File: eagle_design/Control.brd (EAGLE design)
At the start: 55.9 x 63.2 mm, 17 parts, among them K1 G5LE, K2 G5LE, K3 G5LE

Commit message: Did some more PCB design and added some datasheets
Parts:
- removed B1: RECTIFIER-S80, rectifier:TO-269AA
- removed D1, D2, D3: 1N4148DO35-7, diode:DO35-7
- removed D8: CGRM4001-G, diode:SOD-123_MINI-SMA
- removed K1, K2, K3: G5LE, relay:G5LE
- removed SV3, SV4: (no value), con-lstb:MA05-1
- removed T1, T2, T3: (no value), transistor-neu-to92:TO92-EBC
- removed VREG-3.3: (no value), linear-technology:SOT223
- removed VREG-5: TL2575-05, texas:TO-263-5
- added C3, C4: 10uF, rcl:C0805
- added MSP430F1232: F12X2---DW28, TI_MSP430_v16:DW28
- added RN-131C: RN-131G, SparkFun:RN-131G
- added SV1: (no value), con-lstb:MA05-1
- C1: value 100uF -> 0.1uF; device rcl:153CLV-0405 -> rcl:C0805
- C2: value 330uF -> 0.1uF; device rcl:153CLV-0405 -> rcl:C0805
- moved C2 41.5 mm to (36.8, 2.54), turned to 270 degrees
- moved C1 31.9 mm to (5.08, 22.9), turned to 270 degrees
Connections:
- removed net 3.3+: SV3.5, VREG-3.3.3
- removed net 5V+: C2.+, D1.C, D2.C, D3.C, K1.1, K2.1, K3.1, VREG-3.3.1, VREG-5.4
- removed net G: K3.S, SV4.1
- removed net N$1: B1.+, C1.+, VREG-5.1
- removed net N$2: D1.A, K3.2, T1.C
- removed net N$3: D2.A, K2.2, T2.C
- removed net N$4: D8.C, VREG-5.2
- removed net N$5: D3.A, K1.2, T3.C
- removed net N$6: K1.O
- removed net N$7: K2.O
- removed net N$8: K3.O
- removed net VAC+: B1.AC1, K1.P, K2.P, K3.P, SV4.5
- removed net VAC-: SV4.4
- removed net W: K1.S, SV4.3
- removed net Y: K2.S, SV4.2
- new net RESET: RN-131C.RESET
- new net RN-RX: MSP430F1232.15, RN-131C.UART-RX
- new net RN-TX: MSP430F1232.16, RN-131C.UART-TX
- new net VCC: C1.1, C2.1, C3.1, C4.1, MSP430F1232.2, RN-131C.VDD-BATT, RN-131C.VDD-IN, SV1.5
- net AC: now also SV1.2; no longer SV3.2, T2.B
- net FAN: now also SV1.1; no longer SV3.1, T1.B
- net GND: now also C1.2, C2.2, C3.2, C4.2, MSP430F1232.4, RN-131C.3.3-RIN, RN-131C.GND0, RN-131C.GND1, RN-131C.GND2, RN-131C.GND3, RN-131C.GND4, RN-131C.GND5, RN-131C.GND6, RN-131C.GND7, RN-131C.GND8, RN-131C.GND9, SV1.4; no longer B1.-, C1.-, C2.-, D8.A, SV3.4, T1.E, T2.E, T3.E, VREG-3.3.2, VREG-3.3.4, VREG-5.3, VREG-5.5, VREG-5.TAB
- net HEAT: now also SV1.3; no longer SV3.3, T3.B
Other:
- board size 55.9 x 63.2 mm -> 45.7 x 36.5 mm

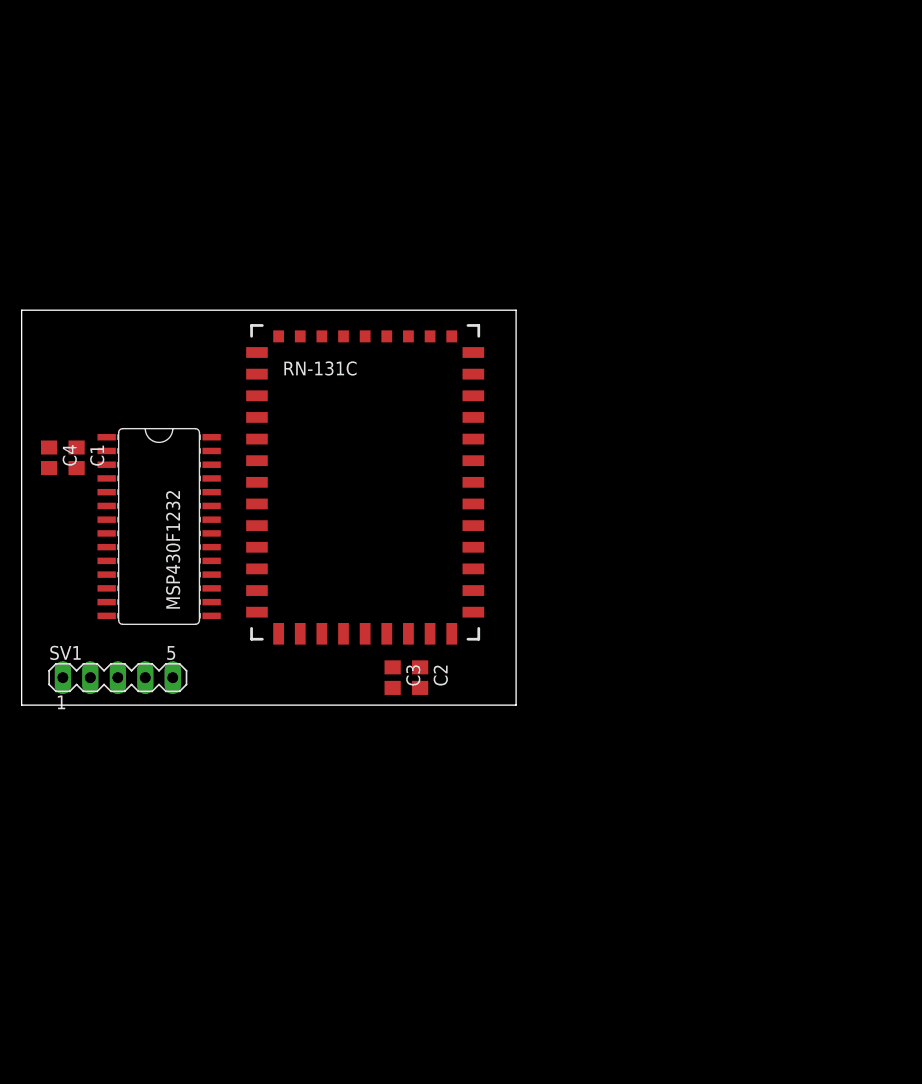
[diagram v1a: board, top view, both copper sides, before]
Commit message: split into three boards and choose new mcu
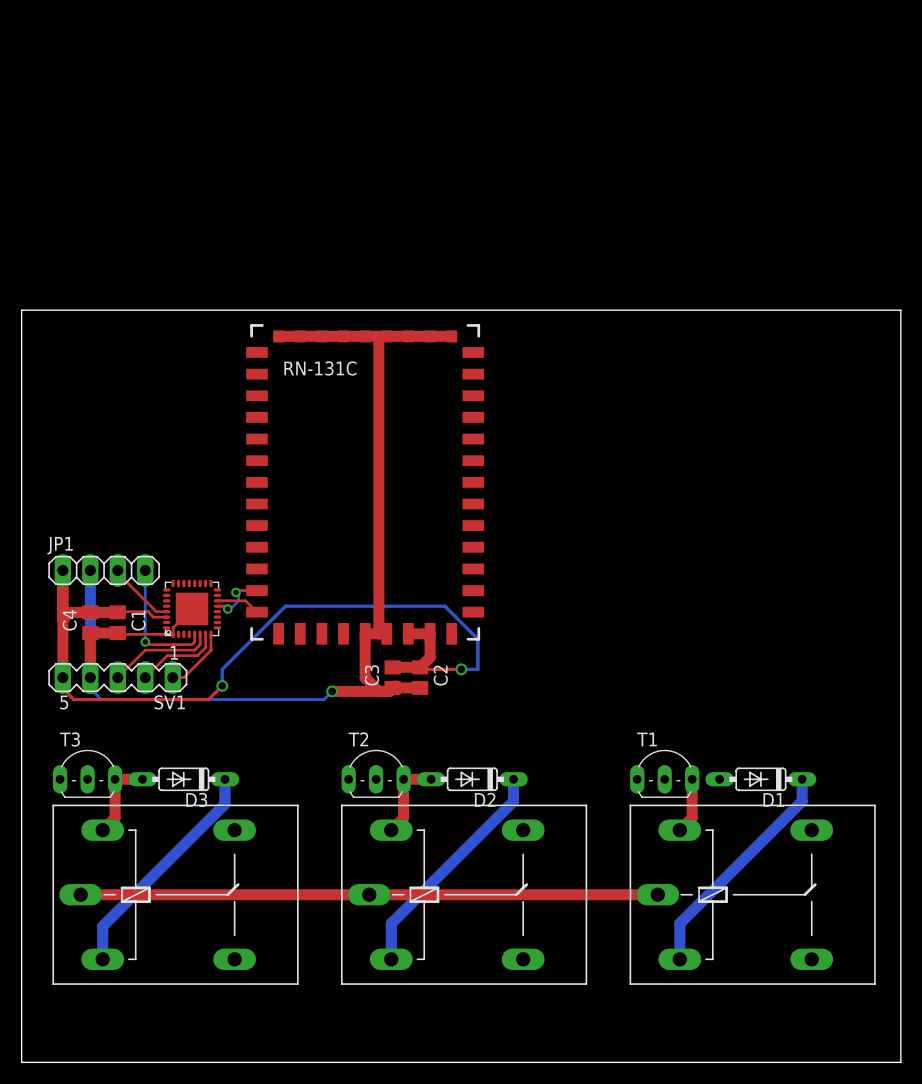
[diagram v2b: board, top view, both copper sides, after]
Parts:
- removed MSP430F1232: F12X2---DW28, TI_MSP430_v16:DW28
- added D1, D2, D3: 1N4148DO35-7, diode:DO35-7
- added JP1: (no value), pinhead:1X04
- added K1, K2, K3: G5LE, relay:G5LE
- added T1, T2, T3: (no value), transistor-neu-to92:TO92-EBC
- added U$1: F21X2---RHB32, TI_MSP430_v16:RHB32
- moved C1 15.7 mm to (8.89, 7.62)
- moved C4 15.7 mm to (6.35, 7.62)
- turned SV1 to 180 degrees
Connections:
- new net 5V+: D1.C, D2.C, D3.C, K1.1, K2.1, K3.1
- new net G: K3.S
- new net N$2: D1.A, K3.2, T1.C
- new net N$3: D2.A, K2.2, T2.C
- new net N$5: D3.A, K1.2, T3.C
- new net N$6: K1.O
- new net N$7: K2.O
- new net N$8: K3.O
- new net RST: JP1.4, U$1.5
- new net TEST: JP1.3, U$1.29
- new net VAC+: K1.P, K2.P, K3.P
- new net W: K1.S
- new net Y: K2.S
- net AC: now also T2.B, U$1.7
- net FAN: now also T1.B, U$1.8
- net GND: now also JP1.2, T1.E, T2.E, T3.E, U$1.1, U$1.TP; no longer MSP430F1232.4
- net HEAT: now also T3.B, U$1.6
- net RN-RX: now also U$1.13; no longer MSP430F1232.15
- net RN-TX: now also U$1.14; no longer MSP430F1232.16
- net VCC: now also JP1.1, U$1.30; no longer MSP430F1232.2
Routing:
- net GND: track 0.00 -> 110.3 mm, vias 0 -> 1
- net VCC: track 0.00 -> 86.0 mm, vias 0 -> 2
- net 5V+: track 0.00 -> 64.0 mm
- net VAC+: track 0.00 -> 53.3 mm
- net RST: track 0.00 -> 12.1 mm, vias 0 -> 1
- net HEAT: track 0.00 -> 9.83 mm
- net AC: track 0.00 -> 7.96 mm
- net N$5: track 0.00 -> 7.71 mm
- net N$3: track 0.00 -> 7.71 mm
- net TEST: track 0.00 -> 6.24 mm
- net FAN: track 0.00 -> 6.08 mm
- net RN-RX: track 0.00 -> 5.27 mm, vias 0 -> 2
- net N$2: track 0.00 -> 5.17 mm
- net RN-TX: track 0.00 -> 4.09 mm
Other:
- board size 45.7 x 36.5 mm -> 81.3 x 69.5 mm

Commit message: removed relays from control
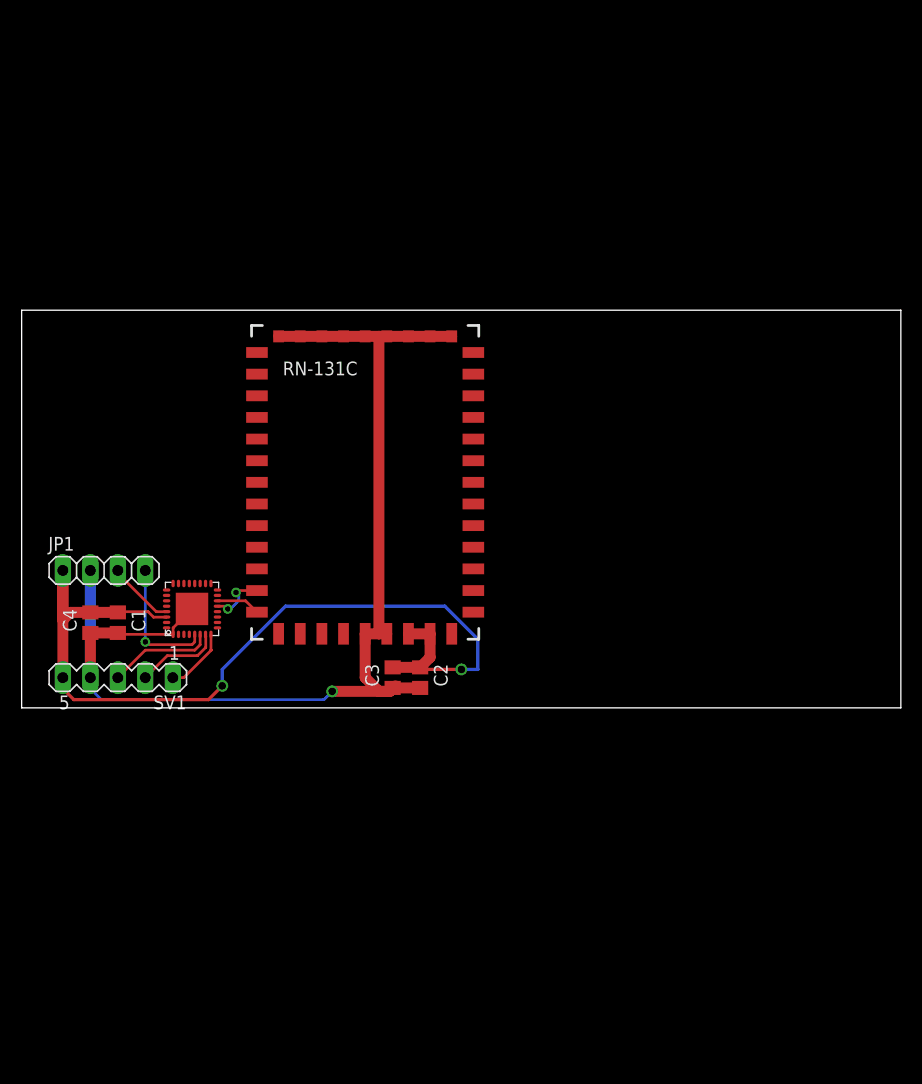
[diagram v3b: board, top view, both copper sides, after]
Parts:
- removed D1, D2, D3: 1N4148DO35-7, diode:DO35-7
- removed K1, K2, K3: G5LE, relay:G5LE
- removed T1, T2, T3: (no value), transistor-neu-to92:TO92-EBC
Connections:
- removed net 5V+: D1.C, D2.C, D3.C, K1.1, K2.1, K3.1
- removed net G: K3.S
- removed net N$2: D1.A, K3.2, T1.C
- removed net N$3: D2.A, K2.2, T2.C
- removed net N$5: D3.A, K1.2, T3.C
- removed net N$6: K1.O
- removed net N$7: K2.O
- removed net N$8: K3.O
- removed net VAC+: K1.P, K2.P, K3.P
- removed net W: K1.S
- removed net Y: K2.S
- net AC: no longer T2.B
- net FAN: no longer T1.B
- net GND: no longer T1.E, T2.E, T3.E
- net HEAT: no longer T3.B
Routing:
- net 5V+: track 64.0 -> 0.00 mm
- net VAC+: track 53.3 -> 0.00 mm
- net N$5: track 7.71 -> 0.00 mm
- net N$3: track 7.71 -> 0.00 mm
- net N$2: track 5.17 -> 0.00 mm
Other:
- board size 81.3 x 69.5 mm -> 81.3 x 36.8 mm
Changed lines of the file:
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@@
 <board>
 <plain>
-<wire x1="0" y1="-33.02" x2="81.26" y2="-33.02" width="0" layer="20"/>
-<wire x1="81.26" y1="-33.02" x2="81.26" y2="36.5" width="0" layer="20"/>
+<wire x1="0" y1="-0.254" x2="81.26" y2="-0.254" width="0" layer="20"/>
+<wire x1="81.26" y1="-0.254" x2="81.26" y2="36.5" width="0" layer="20"/>
 <wire x1="81.26" y1="36.5" x2="0" y2="36.5" width="0" layer="20"/>
-<wire x1="0" y1="36.5" x2="0" y2="-33.02" width="0" layer="20"/>
+<wire x1="0" y1="36.5" x2="0" y2="-0.254" width="0" layer="20"/>
 </plain>
 <attributes>
@@
 <element name="U$1" library="TI_MSP430_v16" package="RHB32" value="F21X2---RHB32" x="15.748" y="8.89" smashed="yes" rot="R90"/>
 <element name="JP1" library="pinhead" package="1X04" value="" x="7.62" y="12.446"/>
-<element name="K1" library="relay" package="G5LE" value="G5LE" x="14.986" y="-17.526" smashed="yes">
-<attribute name="OC_NEWARK" value="unknown" x="14.986" y="-17.526" size="1.778" layer="27" display="off"/>
-<attribute name="MPN" value="" x="14.986" y="-17.526" size="1.778" layer="27" display="off"/>
-<attribute name="MF" value="" x="14.986" y="-17.526" size="1.778" layer="27" display="off"/>
-<attribute name="OC_FARNELL" value="unknown" x="14.986" y="-17.526" size="1.778" layer="27" display="off"/>
-</element>
-<element name="K2" library="relay" package="G5LE" value="G5LE" x="41.656" y="-17.526" smashed="yes">
-<attribute name="OC_NEWARK" value="unknown" x="41.656" y="-17.526" size="1.778" layer="27" display="off"/>
-<attribute name="MPN" value="" x="41.656" y="-17.526" size="1.778" layer="27" display="off"/>
-<attribute name="MF" value="" x="41.656" y="-17.526" size="1.778" layer="27" display="off"/>
-<attribute name="OC_FARNELL" value="unknown" x="41.656" y="-17.526" size="1.778" layer="27" display="off"/>
-</element>
-<element name="K3" library="relay" package="G5LE" value="G5LE" x="68.326" y="-17.526" smashed="yes">
-<attribute name="OC_NEWARK" value="unknown" x="68.326" y="-17.526" size="1.778" layer="27" display="off"/>
-<attribute name="MPN" value="" x="68.326" y="-17.526" size="1.778" layer="27" display="off"/>
-<attribute name="MF" value="" x="68.326" y="-17.526" size="1.778" layer="27" display="off"/>
-<attribute name="OC_FARNELL" value="unknown" x="68.326" y="-17.526" size="1.778" layer="27" display="off"/>
-</element>
-<element name="D1" library="diode" package="DO35-7" value="1N4148DO35-7" x="68.326" y="-6.858" smashed="yes" rot="R180">
-<attribute name="NAME" x="70.612" y="-8.128" size="1.27" layer="25" ratio="10" rot="R180"/>
-</element>
-<element name="D2" library="diode" package="DO35-7" value="1N4148DO35-7" x="41.656" y="-6.858" smashed="yes" rot="R180">
-<attribute name="NAME" x="43.942" y="-8.128" size="1.27" layer="25" ratio="10" rot="R180"/>
-</element>
-<element name="D3" library="diode" package="DO35-7" value="1N4148DO35-7" x="14.986" y="-6.858" smashed="yes" rot="R180">
-<attribute name="NAME" x="17.272" y="-8.128" size="1.27" layer="25" ratio="10" rot="R180"/>
-</element>
-<element name="T1" library="transistor-neu-to92" package="TO92-EBC" value="" x="59.436" y="-5.588"/>
-<element name="T2" library="transistor-neu-to92" package="TO92-EBC" value="" x="32.766" y="-5.588"/>
-<element name="T3" library="transistor-neu-to92" package="TO92-EBC" value="" x="6.096" y="-5.588"/>
 </elements>
 <signals>
@@
 <wire x1="34.036" y1="1.27" x2="34.544" y2="1.778" width="1.016" layer="1"/>
 <wire x1="6.35" y1="12.446" x2="6.35" y2="2.54" width="1.016" layer="16"/>
-<contactref element="T1" pad="E"/>
-<contactref element="T2" pad="E"/>
-<contactref element="T3" pad="E"/>
 <wire x1="35.75" y1="34.082" x2="37.75" y2="34.082" width="0" layer="19" extent="1-1"/>
 <wire x1="33.75" y1="34.082" x2="35.75" y2="34.082" width="0" layer="19" extent="1-1"/>
@@
 <wire x1="27.75" y1="34.082" x2="29.75" y2="34.082" width="0" layer="19" extent="1-1"/>
 <wire x1="25.75" y1="34.082" x2="23.75" y2="34.082" width="0" layer="19" extent="1-1"/>
-<wire x1="30.226" y1="-6.858" x2="27.94" y2="0.508" width="0" layer="19" extent="16-16"/>
-<wire x1="3.556" y1="-6.858" x2="7.366" y2="0.508" width="0" layer="19" extent="16-16"/>
-<wire x1="56.896" y1="-6.858" x2="36.83" y2="1.59" width="0" layer="19" extent="1-1"/>
 </signal>
 <signal name="RESET">
@@
 <wire x1="16.002" y1="5.08" x2="11.43" y2="5.08" width="0.254" layer="1"/>
 <wire x1="11.43" y1="5.08" x2="8.89" y2="2.54" width="0.254" layer="1"/>
-<contactref element="T3" pad="B"/>
-<wire x1="6.096" y1="-6.858" x2="8.89" y2="2.54" width="0" layer="19" extent="1-1"/>
 </signal>
 <signal name="AC">
@@
 <wire x1="16.998" y1="6.54" x2="16.998" y2="6.37" width="0.254" layer="1"/>
 <wire x1="16.998" y1="6.37" x2="17.018" y2="6.35" width="0.254" layer="1"/>
-<contactref element="T2" pad="B"/>
-<wire x1="17.018" y1="5.334" x2="32.766" y2="-6.858" width="0" layer="19" extent="1-1"/>
 </signal>
 <signal name="FAN">
@@
 <wire x1="17.526" y1="5.08" x2="14.986" y2="2.54" width="0.254" layer="1"/>
 <wire x1="14.986" y1="2.54" x2="13.97" y2="2.54" width="0.254" layer="1"/>
-<contactref element="T1" pad="B"/>
-<wire x1="17.526" y1="5.08" x2="59.436" y2="-6.858" width="0" layer="19" extent="1-1"/>
 </signal>
 <signal name="TEST">
@@
 <wire x1="11.43" y1="5.842" x2="11.43" y2="12.446" width="0.254" layer="16"/>
 </signal>
-<signal name="N$2">
-<contactref element="D1" pad="A"/>
-<contactref element="K3" pad="2"/>
-<contactref element="T1" pad="C"/>
-<wire x1="61.976" y1="-6.858" x2="64.516" y2="-6.858" width="0" layer="19" extent="1-1"/>
-<wire x1="61.976" y1="-6.858" x2="61.976" y2="-10.414" width="1.016" layer="1"/>
-<wire x1="61.976" y1="-10.414" x2="60.833" y2="-11.557" width="1.016" layer="1"/>
-</signal>
-<signal name="N$3">
-<contactref element="K2" pad="2"/>
-<contactref element="D2" pad="A"/>
-<contactref element="T2" pad="C"/>
-<wire x1="35.306" y1="-6.858" x2="35.306" y2="-10.414" width="1.016" layer="1"/>
-<wire x1="35.306" y1="-10.414" x2="34.163" y2="-11.557" width="1.016" layer="1"/>
-<wire x1="35.306" y1="-6.858" x2="37.846" y2="-6.858" width="1.016" layer="1"/>
-</signal>
-<signal name="N$5">
-<contactref element="K1" pad="2"/>
-<contactref element="D3" pad="A"/>
-<contactref element="T3" pad="C"/>
-<wire x1="8.636" y1="-6.858" x2="8.636" y2="-10.414" width="1.016" layer="1"/>
-<wire x1="8.636" y1="-10.414" x2="7.493" y2="-11.557" width="1.016" layer="1"/>
-<wire x1="8.636" y1="-6.858" x2="11.176" y2="-6.858" width="1.016" layer="1"/>
-</signal>
-<signal name="VAC+">
-<contactref element="K1" pad="P"/>
-<contactref element="K3" pad="P"/>
-<contactref element="K2" pad="P"/>
-<wire x1="5.461" y1="-17.526" x2="32.131" y2="-17.526" width="1.016" layer="1"/>
-<wire x1="32.131" y1="-17.526" x2="58.801" y2="-17.526" width="1.016" layer="1"/>
-</signal>
-<signal name="5V+">
-<contactref element="D2" pad="C"/>
-<contactref element="K2" pad="1"/>
-<contactref element="D3" pad="C"/>
-<contactref element="K1" pad="1"/>
-<contactref element="K3" pad="1"/>
-<contactref element="D1" pad="C"/>
-<wire x1="34.163" y1="-23.495" x2="34.163" y2="-20.193" width="1.016" layer="16"/>
-<wire x1="34.163" y1="-20.193" x2="45.466" y2="-8.89" width="1.016" layer="16"/>
-<wire x1="45.466" y1="-8.89" x2="45.466" y2="-6.858" width="1.016" layer="16"/>
-<wire x1="45.466" y1="-8.89" x2="60.833" y2="-23.495" width="0" layer="19" extent="16-16"/>
-<wire x1="18.796" y1="-6.858" x2="34.163" y2="-20.193" width="0" layer="19" extent="16-16"/>
-<wire x1="7.493" y1="-23.495" x2="7.493" y2="-20.447" width="1.016" layer="16"/>
-<wire x1="7.493" y1="-20.447" x2="18.796" y2="-9.144" width="1.016" layer="16"/>
-<wire x1="18.796" y1="-9.144" x2="18.796" y2="-6.858" width="1.016" layer="16"/>
-<wire x1="60.833" y1="-23.495" x2="60.833" y2="-20.193" width="1.016" layer="16"/>
-<wire x1="60.833" y1="-20.193" x2="72.136" y2="-8.89" width="1.016" layer="16"/>
-<wire x1="72.136" y1="-8.89" x2="72.136" y2="-6.858" width="1.016" layer="16"/>
-</signal>
-<signal name="W">
-<contactref element="K1" pad="S"/>
-</signal>
-<signal name="Y">
-<contactref element="K2" pad="S"/>
-</signal>
-<signal name="G">
-<contactref element="K3" pad="S"/>
-</signal>
-<signal name="N$6">
-<contactref element="K1" pad="O"/>
-</signal>
-<signal name="N$7">
-<contactref element="K2" pad="O"/>
-</signal>
-<signal name="N$8">
-<contactref element="K3" pad="O"/>
-</signal>
 </signals>
